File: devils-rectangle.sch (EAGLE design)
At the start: 24 parts, among them IC1 74AHC1G125DBV, J3 CORTEX_DEBUG_PTH, J6 USB-MICROB, U1 ATSAMD21G-M, U2 MIC5501-3.0YM5-TR, U3 TPD2S017

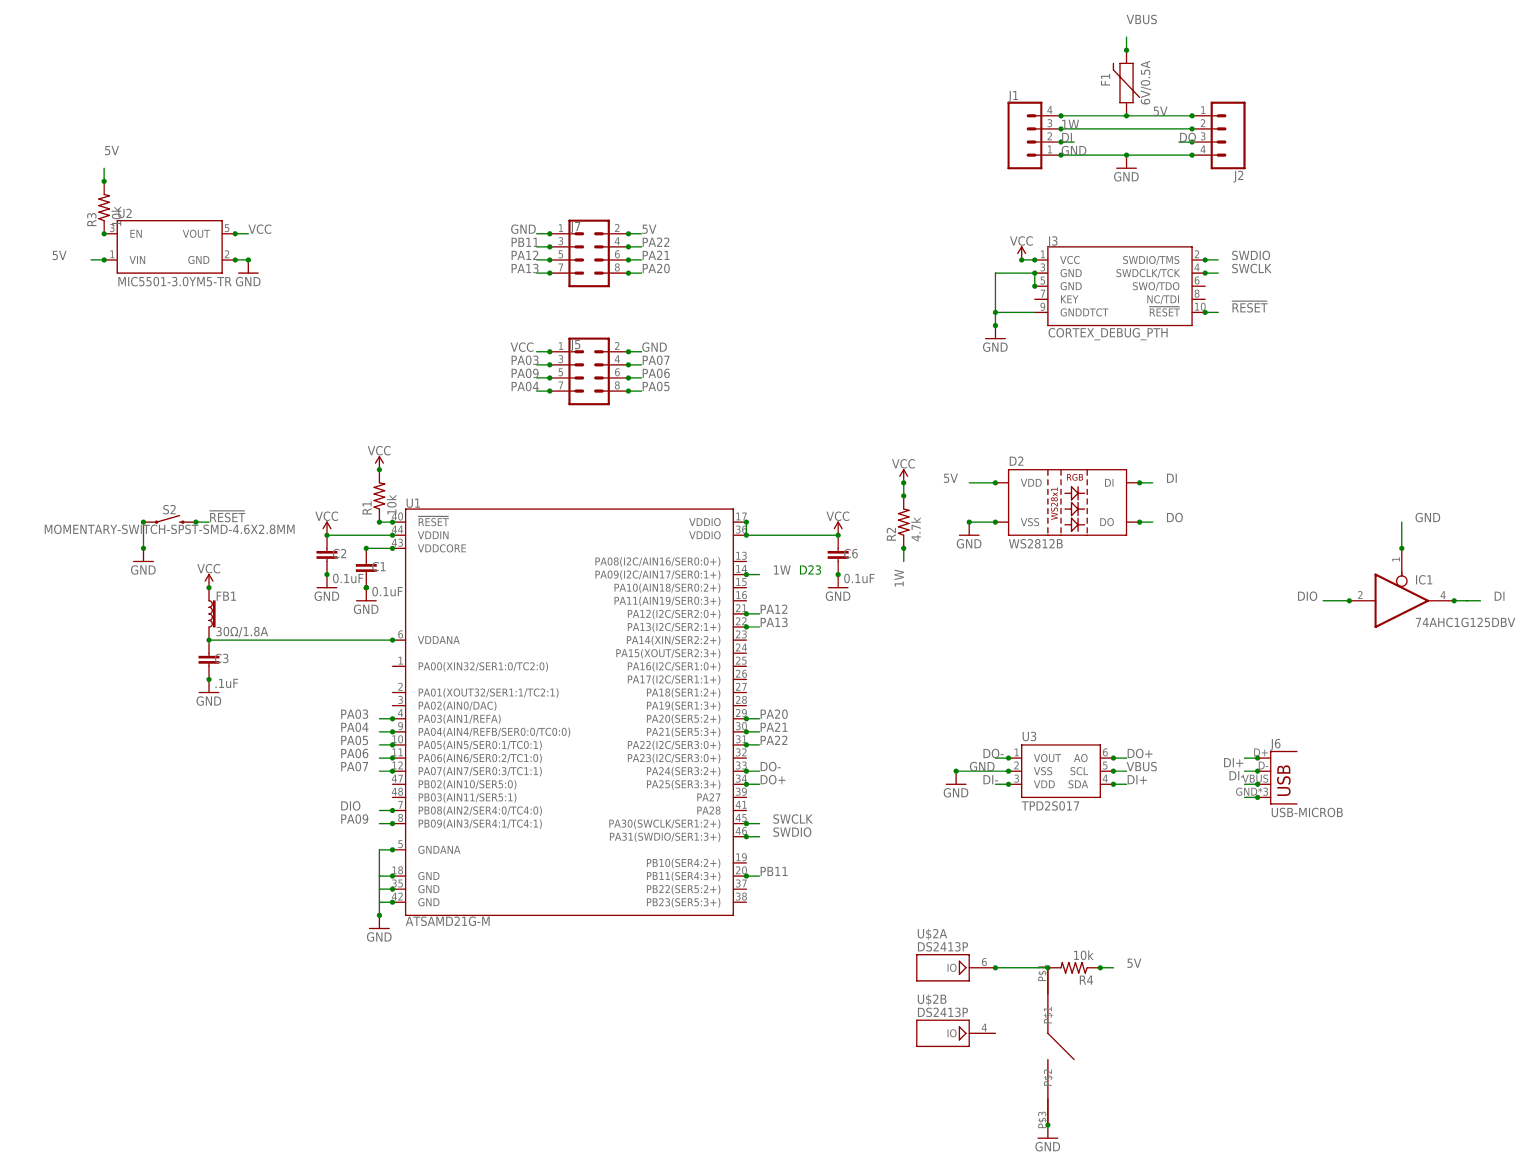
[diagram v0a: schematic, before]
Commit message: fixed errors
fixed errors, added breakout for PIOB on DS2413, updated silk screen
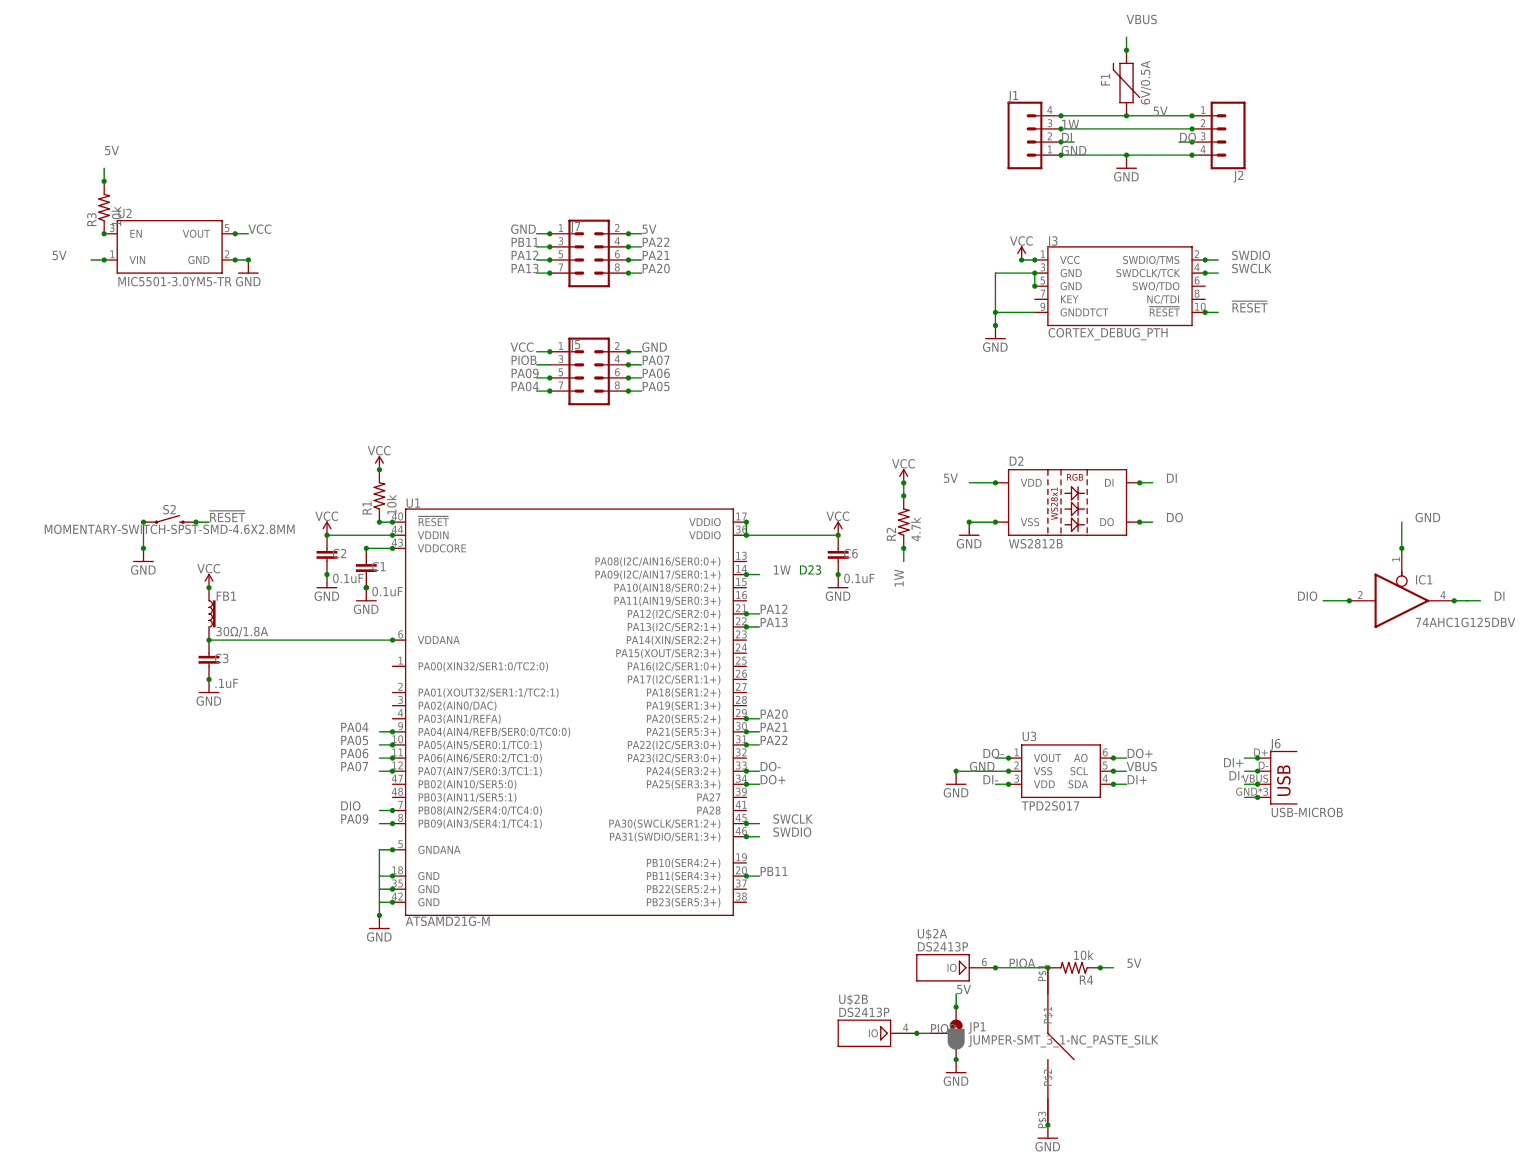
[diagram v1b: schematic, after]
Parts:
- added JP1: JUMPER-SMT_3_1-NC_PASTE_SILK, SparkFun-Jumpers:JUMPER-SMT_3_1-NC_PASTE_SILK
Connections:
- net N$10 renamed PIOA
- removed net PA03: J5.3, U1.PA03(AIN1/REFA)
- new net PIOB: J5.3, JP1.2, U$2B.IO
- net 5V: now also JP1.1
- net GND: now also JP1.3
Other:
- moved on the sheet: U$2B
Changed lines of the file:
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@@
 <?xml version="1.0" encoding="utf-8"?>
 <!DOCTYPE eagle SYSTEM "eagle.dtd">
-<eagle version="9.2.2">
+<eagle version="9.3.2">
 <drawing>
 <settings>
@@
 <part name="GND10" library="supply1" library_urn="urn:adsk.eagle:library:371" deviceset="GND" device=""/>
 <part name="IC1" library="74xx-custom" deviceset="74*1G125" device="DBV" package3d_urn="urn:adsk.eagle:package:2482/1" technology="AHC"/>
+<part name="JP1" library="SparkFun-Jumpers" library_urn="urn:adsk.eagle:library:528" deviceset="JUMPER-SMT_3_1-NC_PASTE" device="_SILK" package3d_urn="urn:adsk.eagle:package:39293/1"/>
+<part name="GND13" library="supply1" library_urn="urn:adsk.eagle:library:371" deviceset="GND" device=""/>
 </parts>
 <sheets>
@@
 <attribute name="NAME" x="261.62" y="66.675" size="1.778" layer="95"/>
 </instance>
-<instance part="U$2" gate="B" x="266.7" y="48.26" smashed="yes">
-<attribute name="VALUE" x="261.62" y="51.435" size="1.778" layer="96"/>
-<attribute name="NAME" x="261.62" y="53.975" size="1.778" layer="95"/>
+<instance part="U$2" gate="B" x="251.46" y="48.26" smashed="yes">
+<attribute name="VALUE" x="246.38" y="51.435" size="1.778" layer="96"/>
+<attribute name="NAME" x="246.38" y="53.975" size="1.778" layer="95"/>
 </instance>
 <instance part="U1" gate="G$1" x="193.04" y="104.14" smashed="yes">
@@
 <attribute name="NAME" x="358.14" y="135.255" size="1.778" layer="95"/>
 <attribute name="VALUE" x="358.14" y="127" size="1.778" layer="96"/>
+</instance>
+<instance part="JP1" gate="G$1" x="269.24" y="48.26" smashed="yes">
+<attribute name="NAME" x="271.78" y="48.641" size="1.778" layer="95" font="vector"/>
+<attribute name="VALUE" x="271.78" y="47.879" size="1.778" layer="96" font="vector" align="top-left"/>
+</instance>
+<instance part="GND13" gate="1" x="269.24" y="40.64" smashed="yes">
+<attribute name="VALUE" x="266.7" y="38.1" size="1.778" layer="96"/>
 </instance>
 </instances>
@@
 <junction x="355.6" y="142.24"/>
 </segment>
+<segment>
+<pinref part="JP1" gate="G$1" pin="3"/>
+<pinref part="GND13" gate="1" pin="GND"/>
+<junction x="269.24" y="43.18"/>
+</segment>
 </net>
 <net name="N$4" class="0">
@@
 <junction x="205.74" y="203.2"/>
 </segment>
+<segment>
+<pinref part="JP1" gate="G$1" pin="1"/>
+<wire x1="269.24" y1="53.34" x2="269.24" y2="55.88" width="0.1524" layer="91"/>
+<junction x="269.24" y="53.34"/>
+<label x="269.24" y="55.88" size="1.778" layer="95"/>
+</segment>
 </net>
 <net name="N$1" class="0">
@@
 </segment>
 </net>
-<net name="N$10" class="0">
+<net name="PIOA" class="0">
 <segment>
 <pinref part="U$2" gate="A" pin="IO"/>
@@
 <junction x="287.02" y="60.96"/>
 <junction x="276.86" y="60.96"/>
+<label x="279.4" y="60.96" size="1.778" layer="95"/>
 </segment>
 </net>
@@
 </segment>
 </net>
-<net name="PA03" class="0">
-<segment>
-<pinref part="U1" gate="G$1" pin="PA03(AIN1/REFA)"/>
-<wire x1="160.02" y1="109.22" x2="157.48" y2="109.22" width="0.1524" layer="91"/>
-<label x="149.86" y="109.22" size="1.778" layer="95"/>
-<junction x="160.02" y="109.22"/>
+<net name="PIOB" class="0">
+<segment>
+<pinref part="U$2" gate="B" pin="IO"/>
+<wire x1="261.62" y1="48.26" x2="264.16" y2="48.26" width="0.1524" layer="91"/>
+<junction x="261.62" y="48.26"/>
+<label x="264.16" y="48.26" size="1.778" layer="95"/>
+<pinref part="JP1" gate="G$1" pin="2"/>
 </segment>
 <segment>
@@
 <wire x1="190.5" y1="177.8" x2="187.96" y2="177.8" width="0.1524" layer="91"/>
 <label x="182.88" y="177.8" size="1.778" layer="95"/>
-<junction x="190.5" y="177.8"/>
-</segment>
-</net>
+</segment>
+</net>
